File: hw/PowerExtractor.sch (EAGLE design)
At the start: 68 parts, among them Q1 BSS84, Q2 BC847SMD, Q3 BC847SMD, Q4 BC847SMD, T1 IRL530N, T2 IRF7416, T3 IRLL014N_, T4 IRLL014N_, U1 ZXCT1086E5TA

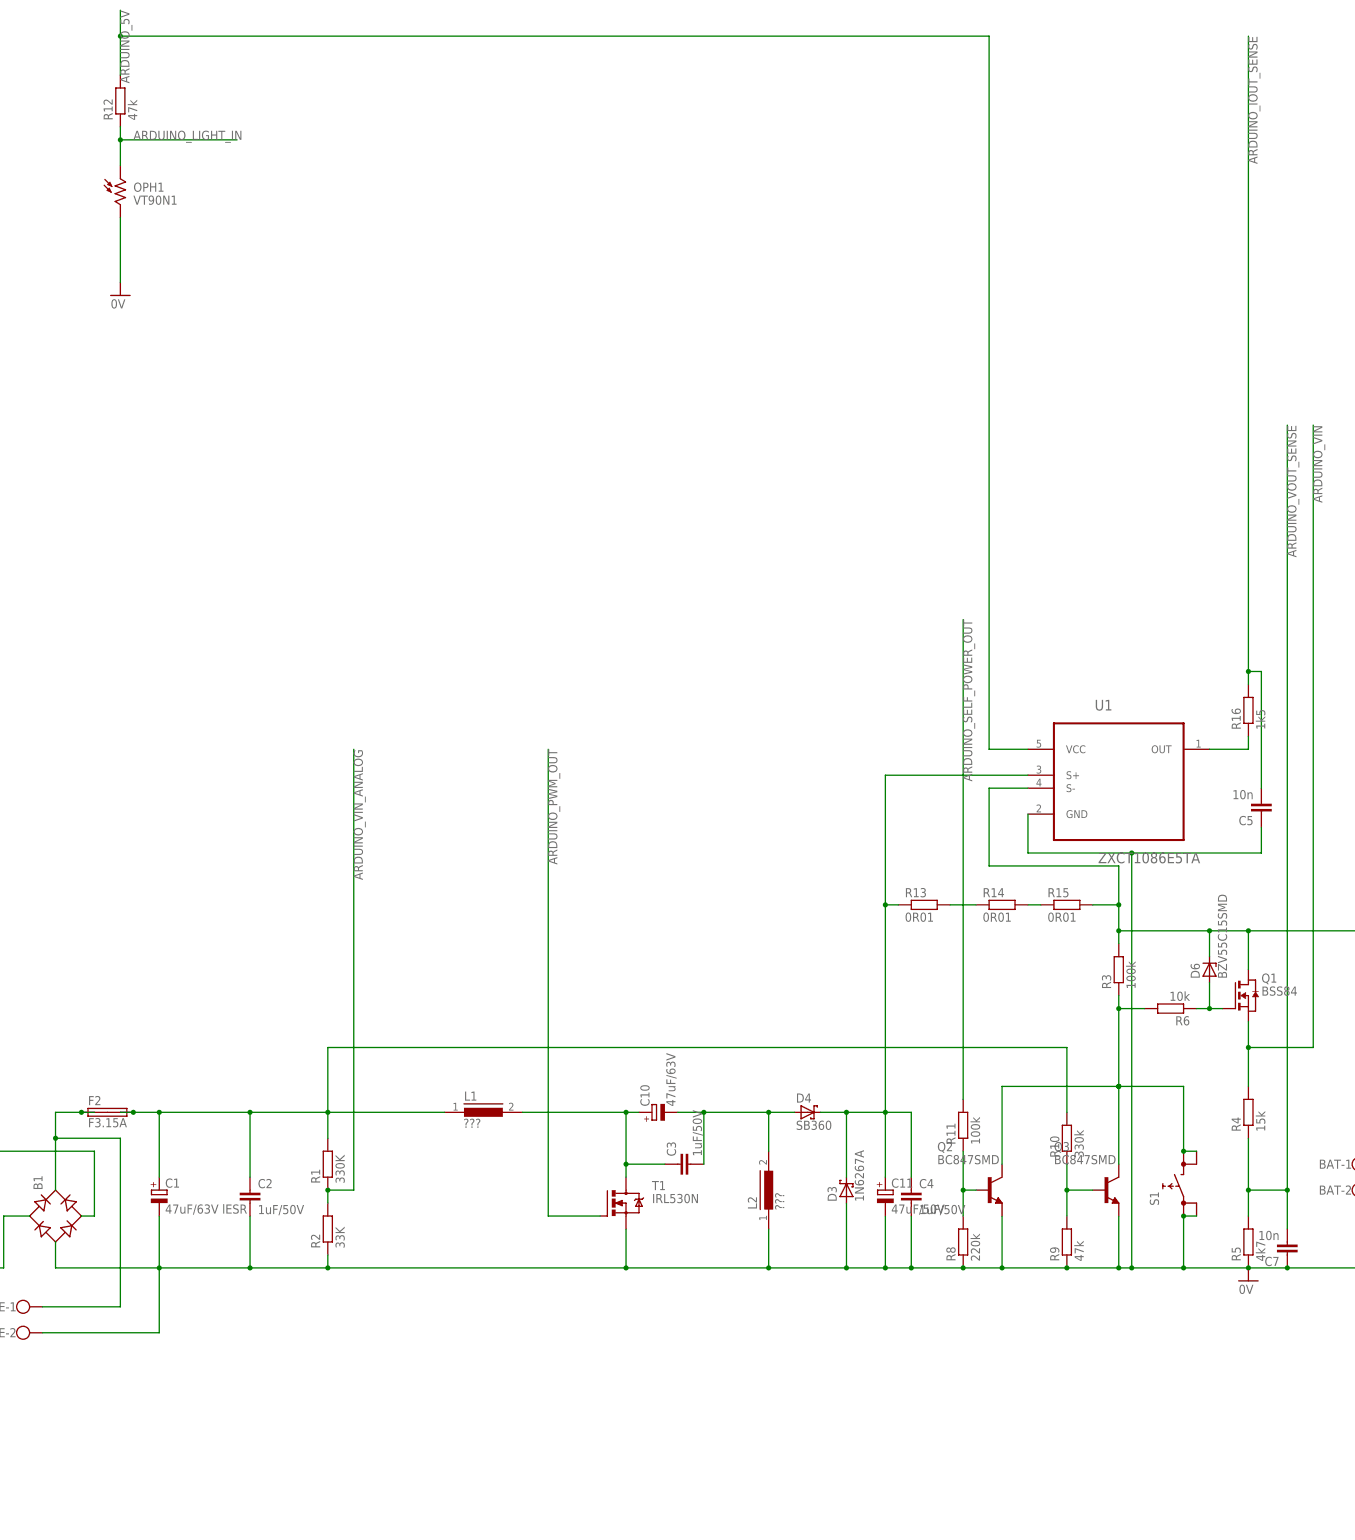
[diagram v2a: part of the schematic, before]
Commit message: Arduino Nano V3 in library
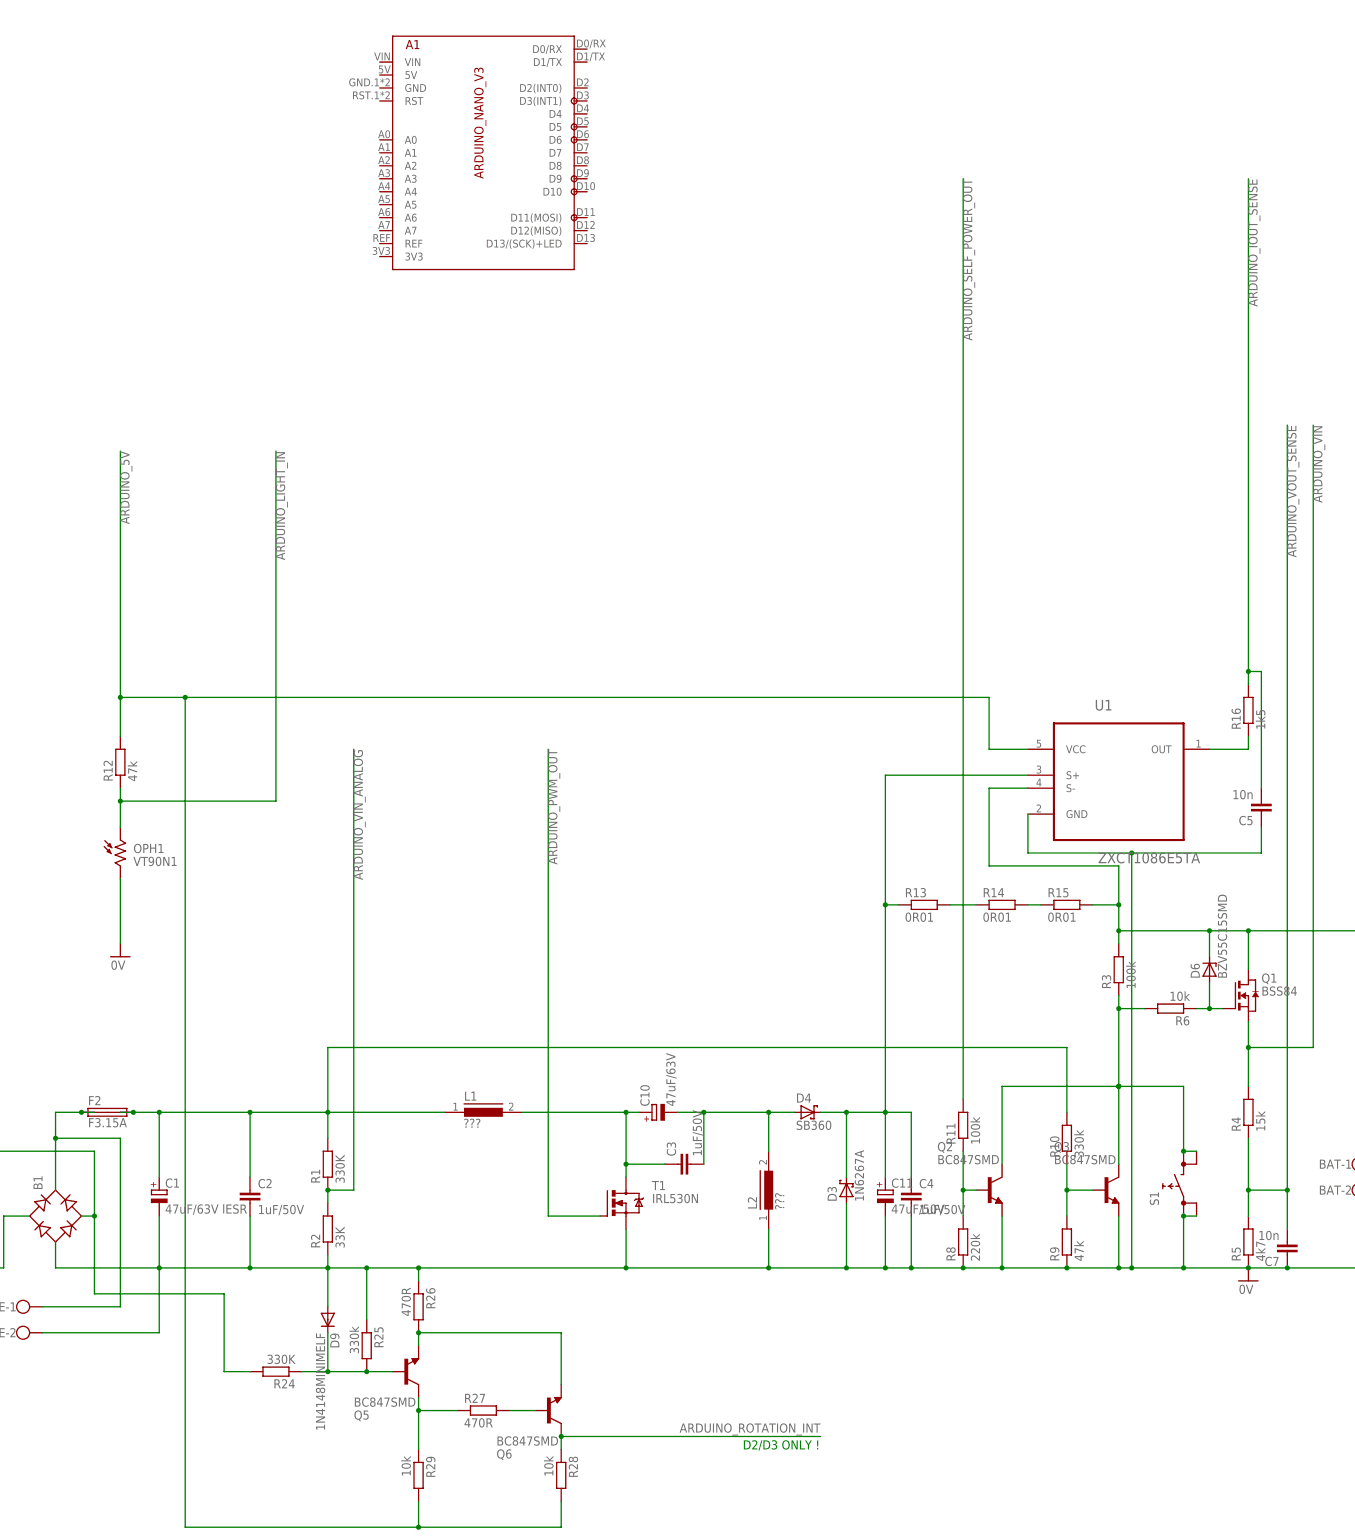
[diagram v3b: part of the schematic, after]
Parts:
- added A1: ARDUINO_NANO_V3, triakcz:ARDUINO_NANO_V3
- added D9: 1N4148MINIMELF, triakcz:1N4148MINIMELF
- added Q5, Q6: BC847SMD, triakcz:BC847SMD
- added R24: 330K, rcl:R-EU_R0805
- added R25: 330k, rcl:R-EU_R0805
- added R26, R27: 470R, rcl:R-EU_R0805
- added R28, R29: 10k, rcl:R-EU_R0805
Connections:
- new net ARDUINO_ROTATION_INT: Q6.C, R28.1
- new net N$29: D9.C, Q5.B, R24.1, R25.2
- new net N$30: Q5.C, R27.1, R29.1
- new net N$31: Q5.E, Q6.E, R26.2
- new net N$32: Q6.B, R27.2
- net ARDUINO_5V: now also R28.2, R29.2
- net GND: now also D9.A, R25.1, R26.1
- net HUB_1: now also R24.2
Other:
- note added: "D2/D3 ONLY !"
- moved on the sheet: OPH1, R12

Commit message: Connected arduino in schematic
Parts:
- added C12, C13, C9: 100N, rcl:C-EUC0805
- added D10: BZV55C05SMD 5V, diode:ZENER-DIODESOD80C
- C5: value 10n -> 100n
- R16: value 1k5 -> 1k
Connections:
- net ARDUINO_5V: now also A1.5V, C13.2
- net ARDUINO_IOUT_SENSE: now also A1.A2, D10.C
- net ARDUINO_LIGHT_IN: now also A1.A0
- net ARDUINO_MAIN_LIGHT_CTRL: now also A1.D5
- net ARDUINO_OUT_CHARGE_OUTPUT_CONTROL: now also A1.D8
- net ARDUINO_OUT_TAIL_LIGHT: now also A1.D6
- net ARDUINO_PWM_OUT: now also A1.D10
- net ARDUINO_ROTATION_INT: now also A1.D2(INT0)
- net ARDUINO_SELF_POWER_OUT: now also A1.D7
- net ARDUINO_VIN: now also A1.VIN
- net ARDUINO_VIN_ANALOG: now also A1.A1
- net ARDUINO_VOUT_SENSE: now also A1.A3
- net GND: now also A1.GND, C12.1, C13.1, C9.1, D10.A
- net N$13: now also C9.2
- net N$5: now also C12.2
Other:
- note added: "Pripojit display"
- note added: "Pripojit klavesnici"
- moved on the sheet: A1

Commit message: Adding latest version
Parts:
- removed 5VOUT: (no value), con-wago-500:W237-102
- removed C12: 100N, rcl:C-EUC0805
- removed D10: BZV55C05SMD 5V, diode:ZENER-DIODESOD80C
- removed Q2: BC847SMD, triakcz:BC847SMD
- removed R8: 220k, rcl:R-EU_R0805
- removed RECOM-785.0-1.0: (no value), v-reg:78XXS
- added DISPLAY: (no value), pinhead:PINHD-1X4
- added IC1: LM358D, linear:LM358D
- added JP10, JP11, JP2, JP3, JP4, JP5, JP6, JP7, JP8, JP9: (no value), pinhead:PINHD-1X1
- added KEYBOARD1: 1GND, pinhead:PINHD-1X5
- added R30, R31: 10k, rcl:R-EU_R0805
- added U2: ZXCT1086E5TA, triakcz:ZXCT1086E5TA
- C5: value 100n -> 100N
- D2: value 1N6285A 39V -> 1N4148MINIMELF; device diode:1N6267A -> triakcz:1N4148MINIMELF
- R15: value 0R01 -> 10k; device rcl:R-EU_M1206 -> rcl:R-EU_R0805
- R16: value 1k -> 10k
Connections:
- removed net 0V: OPH1.2
- removed net ARDUINO_5V: A1.5V, C13.2, R12.2, R28.2, R29.2, U1.VCC
- removed net ARDUINO_IOUT_SENSE: A1.A2, C5.2, D10.C, R16.2
- removed net GND1: R23.2, T4.S
- removed net N$13: C11.+, C4.1, C9.2, D3.C, D4.C, R13.1, U1.S+
- removed net N$15: Q2.B, R11.1, R8.2
- removed net N$23: C6.2, D5.C, F3.2A, F3.2B, R19.2, T2.S, TAIL_LED-2.KL
- new net +3V3: A1.3V3, JP8.1
- new net +5V: A1.5V, C13.2, DISPLAY.1, IC1P.V+, R12.2, R28.2, R29.2, U1.VCC, U2.VCC
- new net ARDUINO_CHARGE_SENSE: A1.A2, IC1A.-IN, IC1A.OUT
- new net BAT+: BAT-2.KL, F1.1A, F1.1B
- new net BAT+FUSED: D6.C, F1.2A, F1.2B, Q1.D, R13.2, R14.1, R15.1, R3.2, R30.1
- new net LIGHTVCC: C6.2, D5.C, F4.2A, F4.2B, R19.2, T2.S, TAIL_LED-2.KL
- new net N$33: A1.D4, KEYBOARD1.2
- new net N$34: A1.A4, DISPLAY.4
- new net N$35: A1.A5, DISPLAY.3
- new net N$36: A1.D12(MISO), KEYBOARD1.5
- new net N$37: A1.D11(MOSI), KEYBOARD1.4
- new net N$38: A1.D1/TX, JP6.1
- new net N$39: A1.D0/RX, JP5.1
- new net N$40: A1.D3(INT1), JP7.1
- new net N$42: A1.A7, JP2.1
- new net N$43: A1.REF, JP3.1
- new net N$44: A1.RST, JP10.1
- new net N$45: A1.D13/(SCK)+LED, JP4.1
- new net N$46: C9.2, R15.2, U2.S+
- new net N$47: C9.1, R31.2, U2.S-
- new net OUT+SENSED: F3.1A, F3.1B, F4.1A, F4.1B, R14.2, R31.1
- new net OUTPUT_TO_SENSE: C11.+, C4.1, D3.C, D4.C, R13.1, R16.1
- net +OUT: now also F3.2A, F3.2B; no longer F4.2A, F4.2B, RECOM-785.0-1.0.IN
- net ARDUINO_VIN: now also JP9.1
- net GND: now also BAT-1.KL, D1.A, DISPLAY.2, IC1P.V-, JP11.1, KEYBOARD1.1, OPH1.2, R23.2, T4.S, U2.GND; no longer BAT-2.KL, C12.1, C5.1, C9.1, D10.A, Q2.E, R8.1
- net HUB2: no longer D2.C
- net HUB_1: no longer D1.C
- net N$1: now also C5.2, R16.2, U1.S+; no longer D1.A, D2.A
- net N$11: now also A1.A6, IC1B.-IN, IC1B.OUT; no longer BAT-1.KL, F1.1A, F1.1B
- net N$12: now also D2.A, R11.1; no longer R14.2, R15.1
- net N$16: now also C5.1, R30.2, U1.S-; no longer R16.1, U1.OUT
- net N$21: now also HEAD_LED-1.KL; no longer HEAD_LED-2.KL
- net N$22: now also HEAD_LED-2.KL; no longer HEAD_LED-1.KL
- net N$26: now also A1.D9, KEYBOARD1.3; no longer 5VOUT-2.KL, RECOM-785.0-1.0.OUT
- net N$28: no longer 5VOUT-1.KL, RECOM-785.0-1.0.GND
- net N$4: now also D2.C
- net N$5: now also IC1A.+IN, U1.OUT; no longer C12.2, D6.C, F1.2A, F1.2B, F3.1A, F3.1B, F4.1A, F4.1B, Q1.D, R15.2, R3.2, U1.S-
- net N$6: no longer Q2.C
- net N$8: now also IC1B.+IN, U2.OUT; no longer R13.2, R14.1
- net VIN: now also D1.C
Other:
- note added: "VCC GND SCL SDA"
- note removed: "Pripojit display"
- note removed: "Pripojit klavesnici"
- moved on the sheet: 12VOUT-1, 12VOUT-2, B1, BAT-1, BAT-2, C1, C11, C4, C5, C6, C7, C8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

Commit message: Routing of board
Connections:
- removed net N$21: HEAD_LED-1.KL, U$1.OUT+
- removed net N$22: HEAD_LED-2.KL, U$1.OUT-
- new net N$13: HEAD_LED-2.KL, U$1.OUT+
- new net N$15: HEAD_LED-1.KL, U$1.OUT-
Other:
- moved on the sheet: HEAD_LED-1, HEAD_LED-2
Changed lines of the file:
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@@
 <instance part="U$1" gate="A" x="528.32" y="38.1"/>
 <instance part="D8" gate="G$1" x="513.08" y="43.18" rot="R180"/>
-<instance part="HEAD_LED" gate="-1" x="556.26" y="45.72" rot="R180"/>
-<instance part="HEAD_LED" gate="-2" x="556.26" y="40.64" rot="R180"/>
+<instance part="HEAD_LED" gate="-1" x="556.26" y="40.64" rot="R180"/>
+<instance part="HEAD_LED" gate="-2" x="556.26" y="45.72" rot="R180"/>
 <instance part="C8" gate="G$1" x="520.7" y="33.02" rot="R180"/>
 <instance part="T3" gate="A" x="589.28" y="33.02"/>
@@
 <junction x="274.32" y="63.5"/>
 <wire x1="279.4" y1="63.5" x2="279.4" y2="243.84" width="0.1524" layer="91"/>
-<label x="287.02" y="185.42" size="1.778" layer="95" rot="R270"/>
+<label x="279.4" y="185.42" size="1.778" layer="95" rot="R270"/>
 <wire x1="279.4" y1="243.84" x2="58.42" y2="243.84" width="0.1524" layer="91"/>
 <wire x1="58.42" y1="243.84" x2="58.42" y2="223.52" width="0.1524" layer="91"/>
@@
 <wire x1="114.3" y1="187.96" x2="119.38" y2="187.96" width="0.1524" layer="91"/>
 <pinref part="A1" gate="G$1" pin="D13/(SCK)+LED"/>
-</segment>
-</net>
-<net name="N$21" class="0">
-<segment>
-<pinref part="U$1" gate="A" pin="OUT+"/>
-<pinref part="HEAD_LED" gate="-1" pin="KL"/>
-<wire x1="551.18" y1="45.72" x2="548.64" y2="45.72" width="0.1524" layer="91"/>
-</segment>
-</net>
-<net name="N$22" class="0">
-<segment>
-<pinref part="U$1" gate="A" pin="OUT-"/>
-<pinref part="HEAD_LED" gate="-2" pin="KL"/>
-<wire x1="551.18" y1="40.64" x2="548.64" y2="40.64" width="0.1524" layer="91"/>
 </segment>
 </net>
@@
 </segment>
 </net>
+<net name="N$13" class="0">
+<segment>
+<pinref part="U$1" gate="A" pin="OUT+"/>
+<pinref part="HEAD_LED" gate="-2" pin="KL"/>
+<wire x1="548.64" y1="45.72" x2="551.18" y2="45.72" width="0.1524" layer="91"/>
+</segment>
+</net>
+<net name="N$15" class="0">
+<segment>
+<pinref part="U$1" gate="A" pin="OUT-"/>
+<wire x1="548.64" y1="40.64" x2="551.18" y2="40.64" width="0.1524" layer="91"/>
+<pinref part="HEAD_LED" gate="-1" pin="KL"/>
+</segment>
+</net>

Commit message: Routing
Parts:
- IC1: value LM358D -> LM358N; device linear:LM358D -> linear:LM358N
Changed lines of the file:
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@@
 <grid distance="0.1" unitdist="inch" unit="inch" style="lines" multiple="1" display="no" altdistance="0.01" altunitdist="inch" altunit="inch"/>
 <layers>
-<layer number="1" name="Top" color="4" fill="1" visible="no" active="no"/>
-<layer number="16" name="Bottom" color="1" fill="1" visible="no" active="no"/>
-<layer number="17" name="Pads" color="2" fill="1" visible="no" active="no"/>
-<layer number="18" name="Vias" color="2" fill="1" visible="no" active="no"/>
-<layer number="19" name="Unrouted" color="6" fill="1" visible="no" active="no"/>
-<layer number="20" name="Dimension" color="15" fill="1" visible="no" active="no"/>
-<layer number="21" name="tPlace" color="7" fill="1" visible="no" active="no"/>
-<layer number="22" name="bPlace" color="7" fill="1" visible="no" active="no"/>
-<layer number="23" name="tOrigins" color="15" fill="1" visible="no" active="no"/>
-<layer number="24" name="bOrigins" color="15" fill="1" visible="no" active="no"/>
-<layer number="25" name="tNames" color="7" fill="1" visible="no" active="no"/>
-<layer number="26" name="bNames" color="7" fill="1" visible="no" active="no"/>
-<layer number="27" name="tValues" color="7" fill="1" visible="no" active="no"/>
-<layer number="28" name="bValues" color="7" fill="1" visible="no" active="no"/>
+<layer number="1" name="Top" color="4" fill="1" visible="yes" active="no"/>
+<layer number="16" name="Bottom" color="1" fill="1" visible="yes" active="no"/>
+<layer number="17" name="Pads" color="2" fill="1" visible="yes" active="no"/>
+<layer number="18" name="Vias" color="2" fill="1" visible="yes" active="no"/>
+<layer number="19" name="Unrouted" color="6" fill="1" visible="yes" active="no"/>
+<layer number="20" name="Dimension" color="15" fill="1" visible="yes" active="no"/>
+<layer number="21" name="tPlace" color="7" fill="1" visible="yes" active="no"/>
+<layer number="22" name="bPlace" color="7" fill="1" visible="yes" active="no"/>
+<layer number="23" name="tOrigins" color="15" fill="1" visible="yes" active="no"/>
+<layer number="24" name="bOrigins" color="15" fill="1" visible="yes" active="no"/>
+<layer number="25" name="tNames" color="7" fill="1" visible="yes" active="no"/>
+<layer number="26" name="bNames" color="7" fill="1" visible="yes" active="no"/>
+<layer number="27" name="tValues" color="7" fill="1" visible="yes" active="no"/>
+<layer number="28" name="bValues" color="7" fill="1" visible="yes" active="no"/>
 <layer number="29" name="tStop" color="7" fill="3" visible="no" active="no"/>
 <layer number="30" name="bStop" color="7" fill="6" visible="no" active="no"/>
@@
 <layer number="35" name="tGlue" color="7" fill="4" visible="no" active="no"/>
 <layer number="36" name="bGlue" color="7" fill="5" visible="no" active="no"/>
-<layer number="37" name="tTest" color="7" fill="1" visible="no" active="no"/>
-<layer number="38" name="bTest" color="7" fill="1" visible="no" active="no"/>
+<layer number="37" name="tTest" color="7" fill="1" visible="yes" active="no"/>
+<layer number="38" name="bTest" color="7" fill="1" visible="yes" active="no"/>
 <layer number="39" name="tKeepout" color="4" fill="11" visible="no" active="no"/>
 <layer number="40" name="bKeepout" color="1" fill="11" visible="no" active="no"/>
@@
 <layer number="44" name="Drills" color="7" fill="1" visible="no" active="no"/>
 <layer number="45" name="Holes" color="7" fill="1" visible="no" active="no"/>
-<layer number="46" name="Milling" color="3" fill="1" visible="no" active="no"/>
-<layer number="47" name="Measures" color="7" fill="1" visible="no" active="no"/>
-<layer number="48" name="Document" color="7" fill="1" visible="no" active="no"/>
-<layer number="49" name="Reference" color="7" fill="1" visible="no" active="no"/>
-<layer number="51" name="tDocu" color="7" fill="1" visible="no" active="no"/>
-<layer number="52" name="bDocu" color="7" fill="1" visible="no" active="no"/>
+<layer number="46" name="Milling" color="3" fill="1" visible="yes" active="no"/>
+<layer number="47" name="Measures" color="7" fill="1" visible="yes" active="no"/>
+<layer number="48" name="Document" color="7" fill="1" visible="yes" active="no"/>
+<layer number="49" name="Reference" color="7" fill="1" visible="yes" active="no"/>
+<layer number="51" name="tDocu" color="7" fill="1" visible="yes" active="no"/>
+<layer number="52" name="bDocu" color="7" fill="1" visible="yes" active="no"/>
 <layer number="91" name="Nets" color="2" fill="1" visible="yes" active="yes"/>
 <layer number="92" name="Busses" color="1" fill="1" visible="yes" active="yes"/>
@@
 <part name="R16" library="rcl" deviceset="R-EU_" device="R0805" value="10k"/>
 <part name="R30" library="rcl" deviceset="R-EU_" device="R0805" value="10k"/>
-<part name="IC1" library="linear" deviceset="LM358" device="D"/>
+<part name="IC1" library="linear" deviceset="LM358" device="N" value="LM358N"/>
 <part name="R14" library="rcl" deviceset="R-EU_" device="M1206" value="0R01"/>
 <part name="U2" library="triakcz" deviceset="ZXCT1086E5TA" device=""/>

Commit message: Refactored layout
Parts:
- removed JP10, JP11, JP2, JP3, JP4, JP5, JP6, JP7, JP8, JP9: (no value), pinhead:PINHD-1X1
- removed S1: (no value), triakcz:TL1105
- added C12: 10n, rcl:C-EUC0805
- added C14: 1uF/50V, rcl:C-EUC0805
- added D10: 1N4148MINIMELF, triakcz:1N4148MINIMELF
- IC1: value LM358N -> LM358D; device linear:LM358N -> linear:LM358D
- R1, R10, R15, R16, R24, R25, R29, R3, R30, R31, R5, R9: device rcl:R-EU_R0805 -> rcl:R-EU_M0805
- R11, R12, R17, R18, R19, R20, R21, R22, R23, R26, R4, R6, R7: device rcl:R-EU_R0805 -> rcl:R-EU_0207/10
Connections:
- removed net N$33: A1.D4, KEYBOARD1.2
- removed net N$38: A1.D1/TX, JP6.1
- removed net N$39: A1.D0/RX, JP5.1
- removed net N$40: A1.D3(INT1), JP7.1
- removed net N$42: A1.A7, JP2.1
- removed net N$43: A1.REF, JP3.1
- removed net N$44: A1.RST, JP10.1
- removed net N$45: A1.D13/(SCK)+LED, JP4.1
- new net N$22: A1.D4, D10.C
- net +3V3: no longer JP8.1
- net ARDUINO_VIN: now also C14.1; no longer JP9.1
- net ARDUINO_VIN_ANALOG: now also C12.2
- net GND: now also C12.1, C14.2; no longer JP11.1, S1.0@A, S1.0@B
- net N$6: now also D10.A, KEYBOARD1.2; no longer S1.1@A, S1.1@B
